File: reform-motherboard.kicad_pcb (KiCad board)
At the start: 4 copper layers, 130 x 100 mm, 188 parts, among them J1 TinyRex-J1-DF40C, J10 TEST_PMIC_ON, J11 TEST_ON, J12 USB_INT_3, J13 Conn_HDMI, J14 Conn_LVDS, J15 USB_INT_2, J16 Conn_LineIn, J17 Conn_LineOut, J18 TRRS, J19 Conn_BOOT, J2 TinyRex-J2-DF40C, J20 Conn_GPIO1, J21 Conn_GPIO2, J22 Conn_PWRON, J23 Conn_RESET, J24 Conn_01x04, J25 Conn_CONSOLE, J26 Conn_Backlight, J3 TinyRex-J3-DF40C, J4 693072010801, J5 USB_A, J6 Barrel_Jack, J7 USB_A, J8 TEST_3V, J9 USB_INT_1, P1 5622-4100-ML, P2 J0G-0003NL, Q1 2N7002, Q2 2N7002, Q3 2N7002, U1 MPCIE-Socket, U10 SGTL5000XNAA3, U11 TPS74801DRCR, U12 SN74LVC1G08DCKR, U13 TXB0104D, U14 CM2020-00TR, U2 MCP73123T-22SI/MF, U3 TPS61235RWLR, U4 AP1501A-33K5G-13, U5 SN74LVC1G14DBVR, U6 TPS74801DRCR, U7 INA260AIPW, U8 TUSB4041IPAPR, U9 TLV71311PDBV, Y1 24MHz

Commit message: manufacturing version 0.1
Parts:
- added G***: LOGO, mnt:mnt, F.Cu at (61.3, 56.2)
- added G***: LOGO, mnt:reform01, F.Cu at (75.2, 58.4)
- added J27: 48099-5701, 48099-5701:MOLEX_48099-5701, F.Cu at (57.7, 76.8)
- U1: footprint mpcie:mpcie-socket -> 67910-5700:MOLEX_67910-5700
- moved U1 10.7 mm to (108.1, 78.6)
- moved U5 0.95 mm to (51.2, 84.6)
- moved R18 0.10 mm to (118.2, 43.7)
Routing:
- net GND: track 421.2 -> 463.6 mm, vias 178 -> 191
- net +5V: track 346.0 -> 386.2 mm, vias 24 -> 33
- net HDMI_CEC_IN: track 67.5 -> 65.8 mm
- net +1V1: track 69.6 -> 68.3 mm, vias 12 -> 11
- net Net-(J19-Pad1): track 31.8 -> 32.8 mm
- net POK_3V3: track 112.3 -> 113.2 mm, vias 6 -> 5
- net Net-(J2-Pad29): track 28.8 -> 28.1 mm
- added copper zone on B.Cu, net GND
- removed copper zone on F.Cu, net +5V

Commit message: reform motherboard 0.1 release
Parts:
- J21: value Conn_GPIO2 -> Conn_01x06; footprint Pin_Headers:Pin_Header_Straight_2x08_Pitch2.00mm -> Pin_Headers:Pin_Header_Straight_1x06_Pitch2.00mm
- moved J21 4.12 mm to (118.0, 108.1)
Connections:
- J21 pad 6: GND -> Net-(J21-Pad6)
- J3 pad 50: Net-(J21-Pad2) -> Net-(J3-Pad50)
- J3 pad 52: Net-(J21-Pad3) -> Net-(J3-Pad52)
- J3 pad 54: Net-(J21-Pad4) -> Net-(J3-Pad54)
- J3 pad 56: Net-(J21-Pad5) -> Net-(J3-Pad56)
- J3 pad 60: Net-(J21-Pad7) -> Net-(J3-Pad60)
- J3 pad 62: Net-(J21-Pad8) -> Net-(J3-Pad62)
- J3 pad 64: Net-(J21-Pad9) -> Net-(J3-Pad64)
- J3 pad 66: Net-(J21-Pad10) -> Net-(J3-Pad66)
- J3 pad 70: Net-(J21-Pad12) -> Net-(J21-Pad2)
- J3 pad 72: Net-(J21-Pad13) -> Net-(J21-Pad3)
- J3 pad 74: Net-(J21-Pad14) -> Net-(J21-Pad4)
- J3 pad 76: Net-(J21-Pad15) -> Net-(J21-Pad5)
- J3 pad 78: Net-(J21-Pad16) -> Net-(J21-Pad6)
- MH5 pad 1: GND -> Net-(MH5-Pad1)
- MH6 pad 1: GND -> Net-(MH6-Pad1)
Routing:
- net Net-(J21-Pad9): track 35.9 -> 0.00 mm, vias 2 -> 0
- net Net-(J21-Pad7): track 35.8 -> 0.00 mm, vias 2 -> 0
- net Net-(J21-Pad8): track 33.8 -> 0.00 mm, vias 2 -> 0
- net Net-(J21-Pad13): track 33.4 -> 0.00 mm, vias 2 -> 0
- net Net-(J21-Pad10): track 32.8 -> 0.00 mm, vias 2 -> 0
- net Net-(J21-Pad15): track 31.7 -> 0.00 mm, vias 2 -> 0
- net Net-(J21-Pad12): track 31.7 -> 0.00 mm, vias 2 -> 0
- net Net-(J21-Pad14): track 30.7 -> 0.00 mm, vias 2 -> 0
- net Net-(J21-Pad16): track 28.9 -> 0.00 mm, vias 2 -> 0
- net Net-(J21-Pad6): track 0.00 -> 26.9 mm, vias 0 -> 1
- net +3V3: track 367.0 -> 354.9 mm, vias 48 -> 43
- net Net-(J21-Pad4): track 41.9 -> 30.0 mm, vias 2 -> 1
- net +1V5: track 76.9 -> 67.0 mm, vias 21 -> 13
- net Net-(J21-Pad5): track 36.2 -> 29.0 mm, vias 2 -> 1
- net GND: track 463.6 -> 458.0 mm, vias 191 -> 183
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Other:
- net class Default: via_dia 0.4 -> 0.3; via_drill 0.3 -> 0.2
- net class PWR: via_dia 0.5 -> 0.4; via_drill 0.4 -> 0.3
- rule via_min_drill: 0.3 -> 0.2
- rule via_min_size: 0.4 -> 0.3

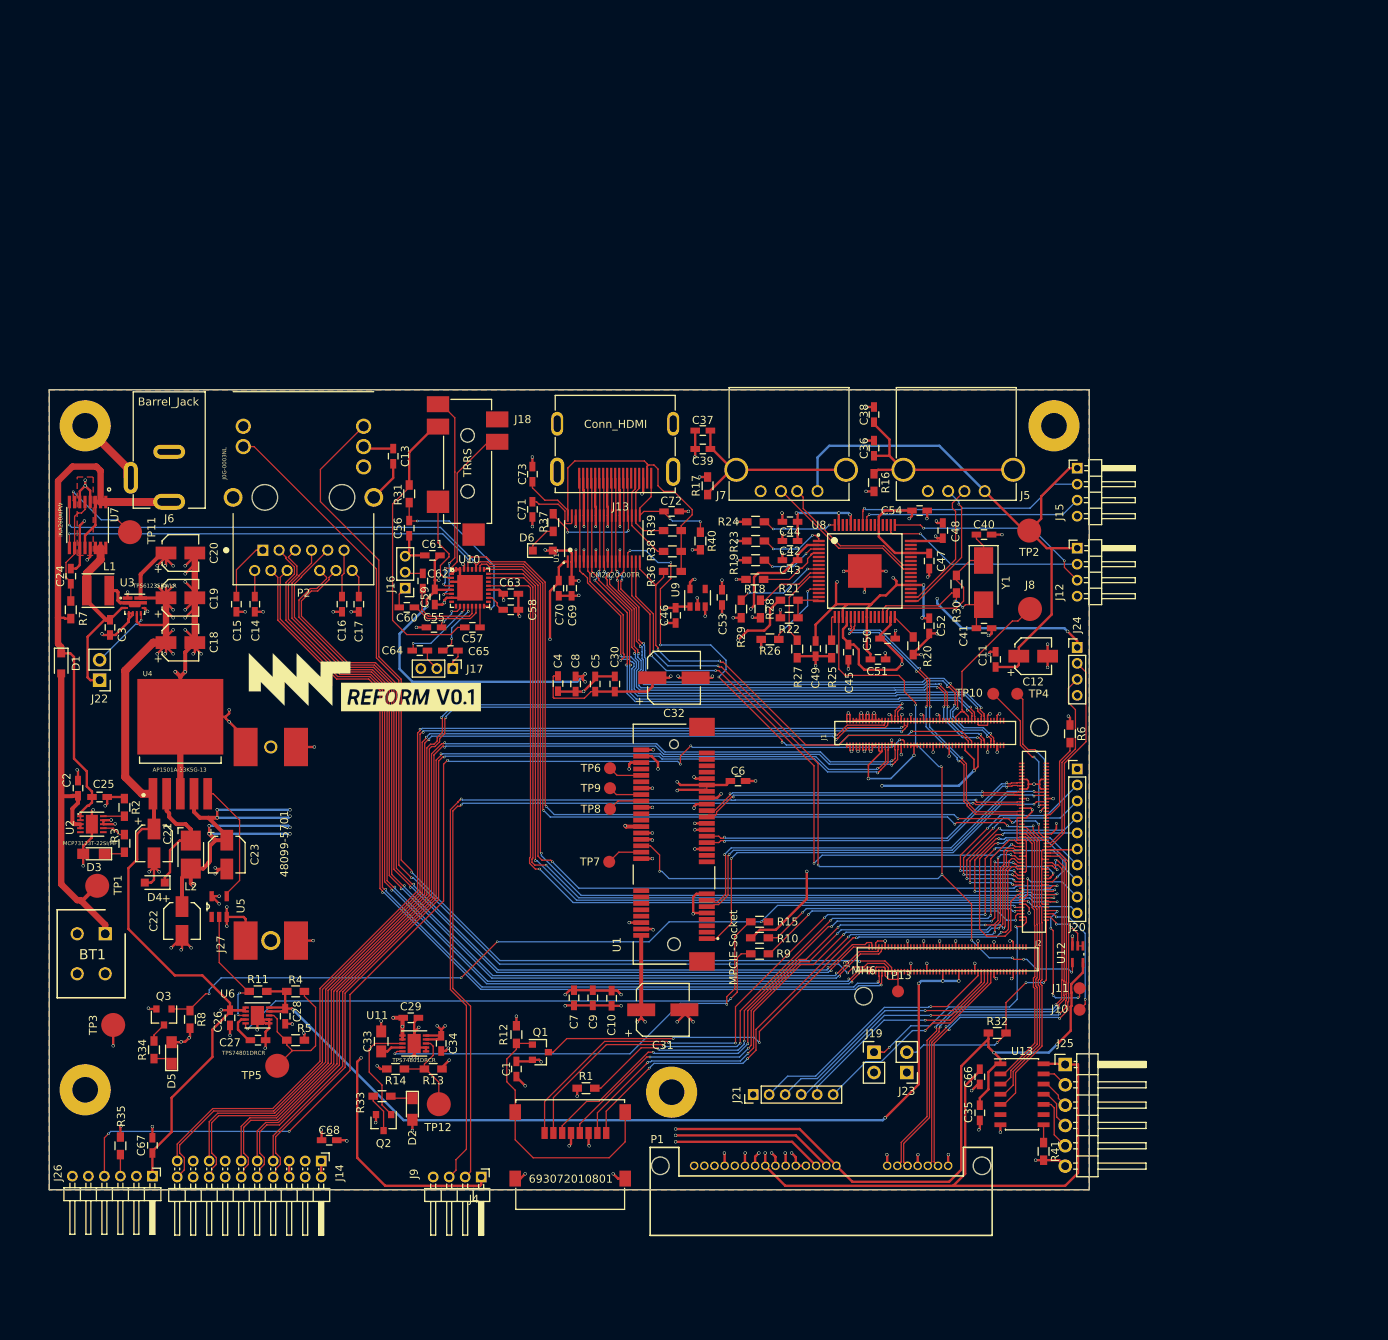
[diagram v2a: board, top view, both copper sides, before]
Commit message: Reform 0.2 mainboard schematics and PCB work in progress
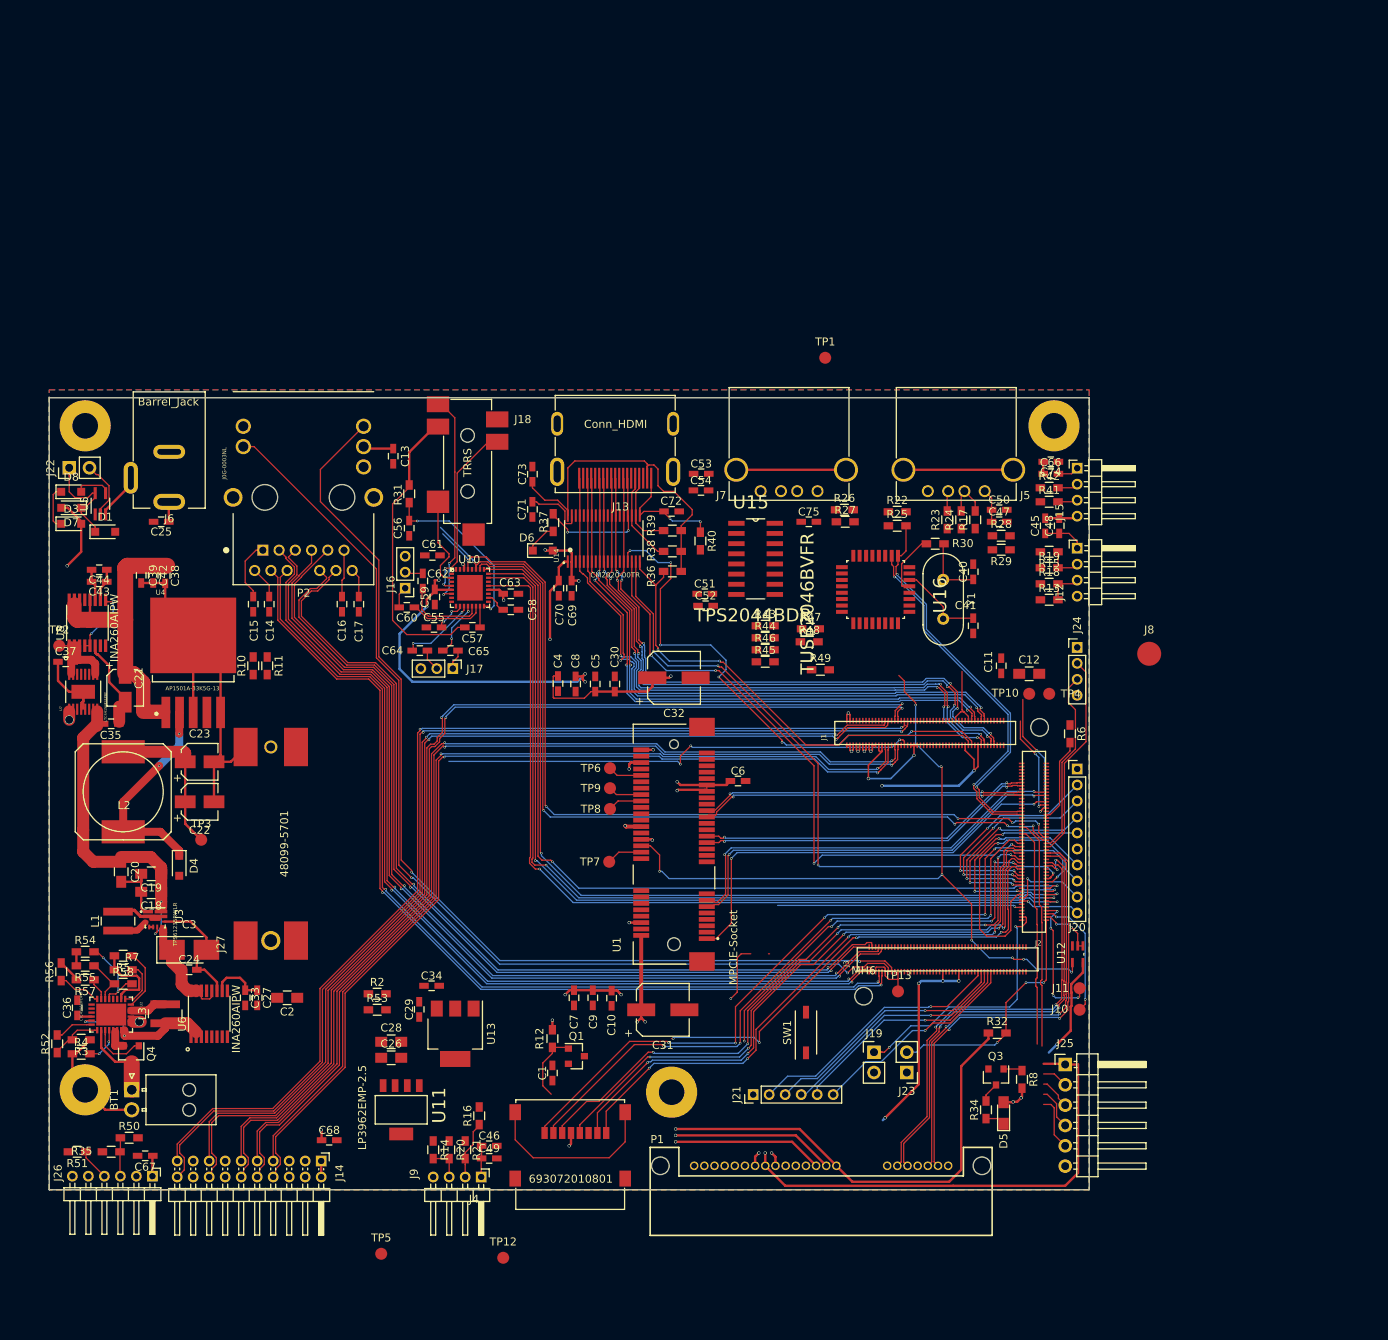
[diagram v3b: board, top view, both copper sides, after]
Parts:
- removed D2: LED_1V5, LEDs:LED_0805_HandSoldering
- removed G***: LOGO, mnt:mnt
- removed G***: LOGO, mnt:reform01
- removed Q2: 2N7002, TO_SOT_Packages_SMD:SOT-23
- removed R1, R9: 0, Resistors_SMD:R_0603_HandSoldering
- removed R33: 240, Resistors_SMD:R_0603_HandSoldering
- removed TP11: PWRMON_ALERT, Measurement_Points:Measurement_Point_Round-SMD-Pad_Big
- removed U9: TLV71311PDBV, TO_SOT_Packages_SMD:SOT-23-5
- added C74: 0.1uF, Capacitors_SMD:C_0603_HandSoldering, F.Cu at (155.2, 29.0)
- added C75: 0.1uF, Capacitors_SMD:C_0603_HandSoldering, F.Cu at (125.0, 36.5)
- added D7: D_Schottky, Diodes_SMD:D_SOD-323_HandSoldering, F.Cu at (32.8, 34.8)
- added D8: D, Diodes_SMD:D_SOD-323_HandSoldering, F.Cu at (32.8, 32.8)
- added L3: 1 uH, Inductors:Inductor_Wurth_MAPI-4020, F.Cu at (44.5, 98.0)
- added Q4: Si5481DU, TO_SOT_Packages_SMD:SOT-23, F.Cu at (40.2, 103.0)
- added R42: 27, Resistors_SMD:R_0603_HandSoldering, F.Cu at (155.0, 32.2)
- added R43: 1.5k, Resistors_SMD:R_0603_HandSoldering, F.Cu at (119.5, 49.5)
- added R44: 1.5k, Resistors_SMD:R_0603_HandSoldering, F.Cu at (119.5, 51.0)
- added R45: 1.5k, Resistors_SMD:R_0603_HandSoldering, F.Cu at (119.5, 54.0)
- added R46: 1.5k, Resistors_SMD:R_0603_HandSoldering, F.Cu at (119.5, 52.5)
- added R47: 0, Resistors_SMD:R_0603_HandSoldering, F.Cu at (125.2, 49.9)
- added R48: 0, Resistors_SMD:R_0603_HandSoldering, F.Cu at (125.0, 51.5)
- added R49: 0, Resistors_SMD:R_0603_HandSoldering, F.Cu at (126.4, 55.0)
- added R50: R0, Resistors_SMD:R_0603_HandSoldering, F.Cu at (40.0, 113.5)
- added R51: R0, Resistors_SMD:R_0603_HandSoldering, F.Cu at (33.5, 115.2)
- added R52: 100k, Resistors_SMD:R_0603_HandSoldering, F.Cu at (31.0, 101.8)
- added R53: 4.7k, Resistors_SMD:R_0603_HandSoldering, F.Cu at (71.0, 97.5)
- added R54: 1.21k, Resistors_SMD:R_0603_HandSoldering, F.Cu at (34.5, 90.2)
- added R55: 1.21k, Resistors_SMD:R_0603_HandSoldering, F.Cu at (34.5, 92.0)
- added R56: 0, Resistors_SMD:R_0603_HandSoldering, F.Cu at (31.5, 92.8)
- added R57: 3.6k, Resistors_SMD:R_0603_HandSoldering, F.Cu at (34.5, 93.8)
- added R58: 0, Resistors_SMD:R_0603_HandSoldering, F.Cu at (39.2, 94.2)
- added SW1: SW_DIP_x01, Buttons_Switches_SMD:SW_DIP_x1_W5.08mm_Slide_Copal_CHS-A, F.Cu at (124.6, 100.3)
- added U15: TPS2044BDR, TPS2044BDR:SOIC127P600X175-16N, F.Cu at (120.7, 45.6)
- added U16: TUSB2046BVFR, TUSB2046BVFR:QFP80P900X900X145-32N, F.Cu at (133.3, 45.0)
- BT1: value Battery_Cell -> Molex 105313-1202; footprint SPTAF:SHDR4W90P500X350_2X2_865X1100X800P -> Connectors_Molex:Molex_NanoFit_1x02x2.50mm_Angled
- C12, C18, C19, C20: footprint Capacitors_SMD:CP_Elec_4x5.8 -> Capacitors_SMD:C_0805_HandSoldering
- C2: value 4.7uF -> 22uF; footprint Capacitors_SMD:C_0603_HandSoldering -> Capacitors_SMD:C_0805_HandSoldering
- C24, C39: value 0.1uF -> 1uF
- C26: value 1uF -> 68uF; footprint Capacitors_SMD:C_0603_HandSoldering -> Capacitors_SMD:C_0805_HandSoldering
- C27: value 4.7uF -> 10uF
- C28: value 10uF -> 33uF; footprint Capacitors_SMD:C_0603_HandSoldering -> Capacitors_SMD:C_0805_HandSoldering
- C3: footprint Capacitors_SMD:C_0603_HandSoldering -> Capacitors_Tantalum_SMD:CP_Tantalum_Case-T_EIA-3528-12_Hand
- C33: value 4.7uF -> 0.1uF; footprint Capacitors_SMD:C_0805_HandSoldering -> Capacitors_SMD:C_0603_HandSoldering
- C34: value 10uF -> 1uF
- C35: value 0.1uF -> 4.7uF
- C36: value 0.001uF -> 0.047uF
- C37: value 0.001uF -> 4.7uF
- C38, C43, C45, C46, C47, C51, C66: value 0.1uF -> 10uF
- C40, C41: value 18pF -> 27pF
- C53: value 1uF -> 10uF
- D3: value LED_CHRG -> D; footprint LEDs:LED_0805_HandSoldering -> Diodes_SMD:D_SOD-323_HandSoldering
- L1: footprint Inductors:Inductor_Taiyo-Yuden_MD-4040 -> Inductors:Inductor_Wurth_MAPI-4020
- L2: footprint Inductors:Inductor_1212 -> Inductors:SELF-WE-PD-XXL
- R10, R7: value 0 -> 4.7k
- R11: value 10k -> 4.7k
- R13: value 2.1k -> 15k
- R14: value 2.4k -> 15k
- R15: value 0 -> 15k
- R16, R17: value 1M -> 15k
- R18, R19, R23, R24, R26, R27: value 4.7k -> 27
- R2: value 1.15k -> 4.7k
- R20: value 9.53k 1% -> 27
- R21: value 90.9 1% -> 27
- R22: value 10k 1% -> 15k
- R25: value 4.7k -> 1.5k
- R28, R29: value 4.7k -> 15k
- R3: value 1k -> 100k
- R30: value 10M -> 1.5k
- R4: value 5.1k -> 499
- R41: value 10k -> 27
- R5: value 2.4k -> 4.7k
- TP1: value TEST_BAT -> TEST_USB_SUSP; footprint Measurement_Points:Measurement_Point_Round-SMD-Pad_Big -> Measurement_Points:Measurement_Point_Round-SMD-Pad_Small
- TP12, TP2, TP3, TP5: footprint Measurement_Points:Measurement_Point_Round-SMD-Pad_Big -> Measurement_Points:Measurement_Point_Round-SMD-Pad_Small
- U11: value TPS74801DRCR -> LP3962EMP-2.5; footprint TPS74801DRCR:SON50P300X300X100-11N -> LP3962EMP-2.5:SOT150P696X180-5N
- U13: value TXB0104D -> TLV1117-15; footprint Housings_SOIC:SOIC-14_3.9x8.7mm_Pitch1.27mm -> TO_SOT_Packages_SMD:SOT-223
- U2: value MCP73123T-22SI/MF -> LTC4156IUFDPBF; footprint MCP73123T-22SI_MF:SON50P300X300X100-11N -> LTC4156IUFDPBF:QFN-28_UFD
- U5: value SN74LVC1G14DBVR -> 74AHC1G14; footprint SN74LVC1G14DBVR:SOT95P280X145-5N -> TO_SOT_Packages_SMD:SOT-353_SC-70-5_Handsoldering
- U6: value TPS74801DRCR -> INA260AIPW; footprint TPS74801DRCR:SON50P300X300X100-11N -> INA260AIPW:SOP65P640X120-16N
- U7: value INA260AIPW -> LTC4415IMSEPBF; footprint INA260AIPW:SOP65P640X120-16N -> LTC4415IMSEPBF:MSOP-16_MSE
- U8: value TUSB4041IPAPR -> INA260AIPW; footprint TUSB4041IPAPR:QFP50P1200X1200X105-65N -> INA260AIPW:SOP65P640X120-16N
- Y1: value 24MHz -> 6MHz; footprint Crystals:Crystal_SMD_Abracon_ABM3-2pin_5.0x3.2mm_HandSoldering -> Crystals:Crystal_HC49-4H_Vertical
- moved TP2 122.1 mm to (31.2, 52.0)
- moved C36 121.7 mm to (33.5, 97.2)
- moved C35 119.0 mm to (37.8, 61.8), turned to 0 degrees
- moved TP1 112.4 mm to (127.0, 16.0)
- moved D5 104.3 mm to (149.3, 110.4)
- moved Q3 104.3 mm to (148.3, 105.9)
- moved R34 104.3 mm to (147.1, 110.0)
- moved R8 104.3 mm to (151.6, 106.2)
- moved U8 97.4 mm to (34.8, 49.1), turned to 90 degrees
- moved R13 96.8 mm to (155.0, 46.2), turned to 0 degrees
- moved R16 93.3 mm to (83.8, 110.8), turned to 90 degrees
- moved C38 90.9 mm to (44.5, 43.2), turned to 270 degrees
- moved C44 86.6 mm to (36.2, 42.5)
- moved C43 86.4 mm to (36.2, 44.0)
- moved R20 85.6 mm to (80.0, 115.0)
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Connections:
- C10 pad 2: +1V5 -> POK_1V5
- C18 pad 1: +5V -> Net-(C18-Pad1)
- C19 pad 1: +5V -> Net-(C18-Pad1)
- C2 pad 1: Net-(BT1-Pad1) -> Net-(C2-Pad1)
- C20 pad 1: +5V -> Net-(C18-Pad1)
- C26 pad 1: +5V -> +3V3
- C27 pad 1: Net-(C27-Pad1) -> +3V3
- C28 pad 1: +2V5 -> POK_2V5
- C29 pad 1: +5V -> POK_2V5
- C3 pad 1: Net-(C3-Pad1) -> Net-(C24-Pad1)
- C33 pad 1: Net-(C33-Pad1) -> +3V3
- C34 pad 1: +1V5 -> POK_1V5
- C35 pad 1: +3V3 -> Net-(C18-Pad1)
- C37 pad 1: Net-(C37-Pad1) -> POK_5V
- C38 pad 1: Net-(C36-Pad1) -> +5V
- C39 pad 1: Net-(C37-Pad1) -> +5V
- C42 pad 1: +1V1 -> +5V
- C44 pad 1: +1V1 -> +3V3
- C45 pad 1: +3V3 -> USB_HUB1_5V
- C46 pad 1: +3V3 -> USB_HUB3_5V
- C47 pad 1: +1V1 -> USB_HUB2_5V
- C48 pad 1: +3V3 -> USB_HUB1_5V
- C49 pad 1: +1V1 -> USB_HUB3_5V
- C50 pad 1: +3V3 -> USB_HUB2_5V
- C51 pad 1: +1V1 -> +5V
- C52 pad 1: +1V1 -> +5V
- C53 pad 1: +1V1 -> +5V
- C54 pad 1: +1V1 -> +5V
- C59 pad 2: +1V5 -> POK_1V5
- C61 pad 2: +1V5 -> +3V3
- C66 pad 1: +5V -> USB_HUB0_5V
- C7 pad 2: +1V5 -> POK_1V5
- C8 pad 2: +1V5 -> POK_1V5
- C9 pad 2: +1V5 -> POK_1V5
- D1 pad 1: Net-(C25-Pad1) -> Net-(D1-Pad1)
- D1 pad 2: Net-(BT1-Pad1) -> Net-(C18-Pad1)
- D3 pad 1: Net-(D3-Pad1) -> BATOFF
- D3 pad 2: GND -> Net-(C25-Pad1)
- J12 pad 1: +5V -> USB_HUB1_5V
- J15 pad 1: +5V -> USB_HUB0_5V
- J22 pad 1: Net-(C3-Pad1) -> Net-(D1-Pad1)
- J25 pad 2: Net-(J25-Pad2) -> UART1_TXD
- J25 pad 3: Net-(J25-Pad3) -> UART1_RXD
- J25 pad 4: Net-(J25-Pad4) -> UART1_RTS
- J25 pad 5: Net-(J25-Pad5) -> UART1_CTS
- J26 pad 4: LVDS0_PWM -> Net-(J26-Pad4)
- J3 pad 48: +2V5 -> POK_2V5
- J3 pad 58: +2V5 -> POK_2V5
- J5 pad 1: +5V -> USB_HUB2_5V
- J5 pad 5: Net-(C36-Pad1) -> GND
- J6 pad 3: JACK_SENSE -> GND
- J7 pad 5: Net-(C37-Pad1) -> GND
- J9 pad 1: +5V -> USB_HUB3_5V
- J9 pad 2: USB0_N -> Net-(J9-Pad2)
- J9 pad 3: USB0_P -> Net-(J9-Pad3)
- L1 pad 1: Net-(C3-Pad1) -> Net-(C24-Pad1)
- R10 pad 1: POK_5V -> I2C3_SDA
- R10 pad 2: +5V -> +3V3
- R11 pad 1: +2V5 -> +3V3
- R11 pad 2: POK_2V5 -> I2C3_SCL
- R13 pad 1: +1V5 -> GND
- R13 pad 2: Net-(R13-Pad2) -> Net-(J12-Pad3)
- R14 pad 1: Net-(R13-Pad2) -> GND
- R14 pad 2: GND -> Net-(J9-Pad3)
- R15 pad 1: Net-(R15-Pad1) -> Net-(J12-Pad2)
- R15 pad 2: POK_3V3 -> GND
- R16 pad 1: Net-(C36-Pad1) -> Net-(J9-Pad2)
- R17 pad 1: Net-(C37-Pad1) -> GND
- R17 pad 2: GND -> Net-(J5-Pad2)
- R18 pad 1: Net-(R18-Pad1) -> USB_HUB1_P
- R18 pad 2: GND -> Net-(J12-Pad3)
- R19 pad 1: Net-(R19-Pad1) -> USB_HUB1_N
- R19 pad 2: GND -> Net-(J12-Pad2)
- R2 pad 1: GND -> +3V3
- R2 pad 2: Net-(R2-Pad2) -> I2C3_SCL
- R20 pad 1: Net-(R20-Pad1) -> USB_HUB3_P
- R20 pad 2: GND -> Net-(J9-Pad3)
- R21 pad 1: +5V -> USB_HUB3_N
- R21 pad 2: Net-(R21-Pad2) -> Net-(J9-Pad2)
- R22 pad 1: Net-(R21-Pad2) -> Net-(J5-Pad3)
- R23 pad 1: Net-(R23-Pad1) -> USB_HUB2_P
- R23 pad 2: GND -> Net-(J5-Pad3)
- R24 pad 1: Net-(R24-Pad1) -> USB_HUB2_N
- R24 pad 2: GND -> Net-(J5-Pad2)
- R25 pad 1: Net-(R25-Pad1) -> +3V3
- R25 pad 2: GND -> USB1_P
- R26 pad 1: Net-(R26-Pad1) -> USB0_P
- R26 pad 2: GND -> Net-(J7-Pad3)
- R27 pad 1: Net-(R27-Pad1) -> USB0_N
- R27 pad 2: GND -> Net-(J7-Pad2)
- R28 pad 1: Net-(R28-Pad1) -> GND
- R28 pad 2: GND -> Net-(J15-Pad3)
- R29 pad 1: Net-(R29-Pad1) -> Net-(J15-Pad2)
- R29 pad 2: +3V3 -> GND
- R3 pad 1: Net-(D3-Pad1) -> GND
- R30 pad 1: Net-(C40-Pad1) -> Net-(R30-Pad1)
- R30 pad 2: Net-(C41-Pad1) -> Net-(C40-Pad1)
- R4 pad 1: +2V5 -> GND
- R41 pad 1: Net-(R41-Pad1) -> USB_HUB0_P
- R41 pad 2: GND -> Net-(J15-Pad3)
- R5 pad 1: Net-(R4-Pad2) -> I2C3_SCL
- R5 pad 2: GND -> +3V3
- R7 pad 1: Net-(C24-Pad1) -> +3V3
- R7 pad 2: Net-(C25-Pad1) -> I2C3_SDA
- TP1 pad 1: Net-(BT1-Pad1) -> Net-(TP1-Pad1)
- TP12 pad 1: Net-(R13-Pad2) -> POK_1V5
- TP2 pad 1: +5V -> POK_5V
- TP5 pad 1: Net-(R4-Pad2) -> POK_2V5
- U1 pad 22: RESET -> RESETn
- U1 pad 28: +1V5 -> POK_1V5
- U1 pad 48: +1V5 -> POK_1V5
- U1 pad 6: +1V5 -> POK_1V5
- U10 pad 30: +1V5 -> POK_1V5
- U10 pad 5: +1V5 -> +3V3
- U11 pad 1: +5V -> +3V3
- U11 pad 2: +5V -> +3V3
- U11 pad 3: POK_1V5 -> POK_2V5
- U11 pad 4: Net-(C33-Pad1) -> GND
- U11 pad 5: Net-(R15-Pad1) -> GND
- U12 pad 4: RESET -> RESETn
- U13 pad 1: +3V3 -> GND
- U13 pad 2: UART1_TXD -> POK_1V5
- U13 pad 3: UART1_RXD -> POK_2V5
- U13 pad 4: UART1_RTS -> (no net)
- U2 pad 1: Net-(C25-Pad1) -> I2C3_SDA
- U2 pad 10: Net-(R2-Pad2) -> Net-(U2-Pad10)
- U2 pad 11: GND -> Net-(U2-Pad11)
- U2 pad 2: Net-(C25-Pad1) -> +3V3
- U2 pad 3: Net-(BT1-Pad1) -> Net-(U2-Pad3)
- U2 pad 4: Net-(BT1-Pad1) -> Net-(U2-Pad4)
- U2 pad 7: Net-(R3-Pad2) -> Net-(R57-Pad1)
- U2 pad 8: GND -> Net-(R56-Pad1)
- U2 pad 9: GND -> Net-(U2-Pad9)
- U3 pad 3: Net-(C3-Pad1) -> Net-(C24-Pad1)
- U3 pad 6: +5V -> Net-(C18-Pad1)
- U3 pad 7: PWRON -> Net-(C24-Pad1)
- U3 pad 9: +5V -> Net-(C18-Pad1)
- U4 pad 5: Net-(U4-Pad5) -> GND
- U5 pad 1: Net-(U5-Pad1) -> (no net)
- U5 pad 2: POK_2V5 -> PWRON
- U5 pad 4: Net-(U4-Pad5) -> Net-(D8-Pad2)
- U5 pad 5: +5V -> Net-(D1-Pad1)
- U6 pad 1: +5V -> Net-(C2-Pad1)
- U6 pad 10: +2V5 -> +3V3
- U6 pad 2: +5V -> Net-(C2-Pad1)
- U6 pad 3: POK_2V5 -> Net-(C2-Pad1)
- U6 pad 4: Net-(C27-Pad1) -> I2C3_SCL
- U6 pad 5: Net-(R9-Pad1) -> I2C3_SDA
- U6 pad 7: GND -> Net-(U6-Pad7)
- U6 pad 8: Net-(R4-Pad2) -> I2C3_SDA
- U6 pad 9: +2V5 -> I2C3_SCL
- U7 pad 10: Net-(C24-Pad1) -> POK_5V
- U7 pad 11: GND -> Net-(U7-Pad11)
- U7 pad 12: Net-(C25-Pad1) -> Net-(U7-Pad12)
- U7 pad 13: GND -> Net-(U7-Pad13)
- U7 pad 14: Net-(C3-Pad1) -> Net-(U7-Pad14)
- U7 pad 15: Net-(C3-Pad1) -> POK_5V
- U7 pad 16: Net-(C3-Pad1) -> POK_5V
- U7 pad 3: Net-(C25-Pad1) -> PWRON
- U7 pad 5: Net-(C24-Pad1) -> GND
- U7 pad 6: GND -> BATOFF
- U7 pad 7: Net-(TP11-Pad1) -> Net-(C18-Pad1)
- U7 pad 8: I2C3_SDA -> Net-(C18-Pad1)
- U7 pad 9: I2C3_SCL -> POK_5V
- U8 pad 1: Net-(R23-Pad1) -> POK_5V
- U8 pad 10: Net-(R27-Pad1) -> +3V3
- U8 pad 11: Net-(U8-Pad11) -> GND
- U8 pad 12: Net-(U8-Pad12) -> +5V
- U8 pad 13: Net-(R26-Pad1) -> Net-(U8-Pad13)
- U8 pad 14: Net-(U8-Pad14) -> +5V
- U8 pad 15: Net-(U8-Pad15) -> +5V
- U8 pad 16: Net-(R21-Pad2) -> +5V
- U8 pad 2: +3V3 -> POK_5V
- U8 pad 3: Net-(R19-Pad1) -> POK_5V
- U8 pad 4: Net-(R18-Pad1) -> I2C3_SCL
- U8 pad 5: Net-(U8-Pad5) -> I2C3_SCL
- U8 pad 6: Net-(U8-Pad6) -> GND
- U8 pad 8: Net-(R29-Pad1) -> I2C3_SDA
- U8 pad 9: Net-(R28-Pad1) -> I2C3_SCL
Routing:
- net GND: track 458.0 -> 154.5 mm, vias 183 -> 0
- net +5V: track 385.9 -> 144.6 mm, vias 31 -> 11
- net USB0_P: track 120.0 -> 0.00 mm, vias 2 -> 0
- net USB0_N: track 118.5 -> 0.00 mm, vias 2 -> 0
- net +3V3: track 354.9 -> 237.2 mm, vias 43 -> 21
- net +2V5: track 115.8 -> 0.00 mm, vias 5 -> 0
- net RESET: track 107.5 -> 0.00 mm, vias 8 -> 0
- net RESETn: track 0.00 -> 93.1 mm, vias 0 -> 8
- net LVDS0_PWM: track 142.7 -> 59.7 mm, vias 6 -> 3
- net POK_3V3: track 113.2 -> 33.1 mm, vias 5 -> 1
- net Net-(R9-Pad1): track 70.1 -> 0.00 mm, vias 2 -> 0
- net +1V1: track 67.1 -> 0.00 mm, vias 10 -> 0
- net +1V5: track 67.0 -> 0.00 mm, vias 13 -> 0
- net Net-(R15-Pad1): track 56.9 -> 0.00 mm, vias 2 -> 0
- net I2C3_SDA: track 160.1 -> 116.8 mm, vias 6 -> 5
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- removed copper zone on Power.Cu, net +1V1
- removed copper zone on Power.Cu, net +3V3
- removed copper zone on Power.Cu, net +5V
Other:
- board size 130 x 100 mm -> 130 x 99 mm
- board text removed: "1V5"
- board text removed: "3V3"

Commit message: Reform 0.2 main PCB routing WIP, 164 nets to go
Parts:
- moved C11 24.0 mm to (173.0, 53.8)
- moved C12 19.9 mm to (172.2, 57.8)
- moved C2 17.3 mm to (43.8, 102.5), turned to 270 degrees
- moved C53 16.1 mm to (127.0, 35.0)
- moved C54 16.0 mm to (127.0, 36.5)
- moved R48 14.9 mm to (130.0, 37.5), turned to 270 degrees
- moved R2 14.5 mm to (57.2, 100.2)
- moved R53 14.5 mm to (57.2, 102.0)
- moved R47 10.8 mm to (127.0, 39.2)
- moved R43 10.1 mm to (126.8, 42.5), turned to 270 degrees
- moved R49 8.66 mm to (135.0, 54.0), turned to 90 degrees
- moved C75 8.48 mm to (133.2, 38.2), turned to 180 degrees
- moved R26 8.00 mm to (121.5, 36.2), turned to 90 degrees
- moved C28 7.08 mm to (78.0, 106.2)
- moved R44 6.96 mm to (126.0, 48.5), turned to 90 degrees
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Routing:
- net USB_HUB3_P: track 0.00 -> 105.4 mm, vias 0 -> 2
- net USB_HUB3_N: track 0.00 -> 104.3 mm, vias 0 -> 2
- net USB_HUB3_5V: track 3.92 -> 104.4 mm, vias 0 -> 2
- net LVDS0_PWM: track 59.7 -> 135.0 mm, vias 3 -> 4
- net POK_2V5: track 26.4 -> 101.1 mm, vias 4 -> 3
- net USB0_P: track 0.00 -> 61.8 mm, vias 0 -> 2
- net USB0_N: track 0.00 -> 61.8 mm, vias 0 -> 2
- net +3V3: track 237.2 -> 187.9 mm, vias 21 -> 17
- net GND: track 154.5 -> 196.8 mm
- net USB_HUB2_5V: track 4.19 -> 39.7 mm, vias 0 -> 2
- net USB_HUB1_N: track 0.00 -> 33.2 mm, vias 0 -> 2
- net USB_HUB1_P: track 0.00 -> 32.5 mm, vias 0 -> 2
- net USB_HUB0_N: track 0.00 -> 30.1 mm, vias 0 -> 2
- net USB_HUB0_P: track 0.00 -> 30.0 mm, vias 0 -> 2
- net Net-(R45-Pad2): track 0.00 -> 28.3 mm, vias 0 -> 2
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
